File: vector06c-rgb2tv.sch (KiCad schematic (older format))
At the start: 77 parts, among them J1 Conn_01x09, Q1 4.43, U1 CXA2075M, U2 7400, U3 7474, U4 74HC240

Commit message: rename project files, fix Improver's nick
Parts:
- TP1, TP10, TP11, TP12, TP13, TP14, TP15, TP16, TP17, TP18, TP19, TP2, TP3, TP4, TP5, TP6, TP7, TP8, TP9: footprint improve-rgb2tv:PAD-150-60 -> vector06c-rgb2tv:PAD-150-60
- U1: symbol improve-rgb2tv-symbols:CXA2075M -> vector06c-rgb2tv-symbols:CXA2075M
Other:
- note removed: "<-- funny value"
- note removed: "^-- funny value"
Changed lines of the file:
@@
 EESchema Schematic File Version 4
-LIBS:improve-rgb2tv-cache
+LIBS:vector06c-rgb2tv-cache
 EELAYER 29 0
 EELAYER END
@@
 F 0 "TP3" V 1500 4700 50  0001 C CNN
 F 1 "9D5" V 1400 4800 50  0000 L CNN
-F 2 "improve-rgb2tv:PAD-150-60" H 1600 4600 50  0001 C CNN
+F 2 "vector06c-rgb2tv:PAD-150-60" H 1600 4600 50  0001 C CNN
 F 3 "~" H 1600 4600 50  0001 C CNN
 	1    1400 4600
@@
 F 0 "TP4" V 1500 5700 50  0001 C CNN
 F 1 "4D3" V 1400 5800 50  0000 L CNN
-F 2 "improve-rgb2tv:PAD-150-60" H 1600 5600 50  0001 C CNN
+F 2 "vector06c-rgb2tv:PAD-150-60" H 1600 5600 50  0001 C CNN
 F 3 "~" H 1600 5600 50  0001 C CNN
 	1    1400 5600
@@
 F 0 "TP5" V 1500 6000 50  0001 C CNN
 F 1 "6D3" V 1400 6100 50  0000 L CNN
-F 2 "improve-rgb2tv:PAD-150-60" H 1600 5900 50  0001 C CNN
+F 2 "vector06c-rgb2tv:PAD-150-60" H 1600 5900 50  0001 C CNN
 F 3 "~" H 1600 5900 50  0001 C CNN
 	1    1400 5900
@@
 F 0 "TP2" V 1500 4300 50  0001 C CNN
 F 1 "12D4" V 1400 4400 50  0000 L CNN
-F 2 "improve-rgb2tv:PAD-150-60" H 1600 4200 50  0001 C CNN
+F 2 "vector06c-rgb2tv:PAD-150-60" H 1600 4200 50  0001 C CNN
 F 3 "~" H 1600 4200 50  0001 C CNN
 	1    1400 4200
@@
 F 0 "TP1" V 1500 4150 50  0001 C CNN
 F 1 "8D8" V 1400 4250 50  0000 L CNN
-F 2 "improve-rgb2tv:PAD-150-60" H 1600 4050 50  0001 C CNN
+F 2 "vector06c-rgb2tv:PAD-150-60" H 1600 4050 50  0001 C CNN
 F 3 "~" H 1600 4050 50  0001 C CNN
 	1    1400 4050
@@
 F 0 "TP6" V 4950 4250 50  0001 C CNN
 F 1 "SYNC" V 4850 4350 50  0000 L CNN
-F 2 "improve-rgb2tv:PAD-150-60" H 5050 4150 50  0001 C CNN
+F 2 "vector06c-rgb2tv:PAD-150-60" H 5050 4150 50  0001 C CNN
 F 3 "~" H 5050 4150 50  0001 C CNN
 	1    4850 4150
@@
 Connection ~ 7050 1350
 $Comp
-L improve-rgb2tv-symbols:CXA2075M U1
+L vector06c-rgb2tv-symbols:CXA2075M U1
 U 1 1 5EEEF62F
 P 7150 2800
@@
 F 0 "TP7" V 9550 2600 50  0001 C CNN
 F 1 "CVOUT" V 9450 2700 50  0000 L CNN
-F 2 "improve-rgb2tv:PAD-150-60" H 9650 2500 50  0001 C CNN
+F 2 "vector06c-rgb2tv:PAD-150-60" H 9650 2500 50  0001 C CNN
 F 3 "~" H 9650 2500 50  0001 C CNN
 	1    9450 2500
@@
 Wire Wire Line
 	6550 5700 6550 5650
-Text Notes 7250 5150 0    50   ~ 0
-<-- funny value
-Text Notes 8050 3250 0    50   ~ 0
-^-- funny value
 Wire Wire Line
 	8950 5200 8950 5100
@@
 F 0 "TP10" V 1250 1350 50  0001 C CNN
 F 1 "GND" V 1150 1450 50  0000 L CNN
-F 2 "improve-rgb2tv:PAD-150-60" H 1350 1250 50  0001 C CNN
+F 2 "vector06c-rgb2tv:PAD-150-60" H 1350 1250 50  0001 C CNN
 F 3 "~" H 1350 1250 50  0001 C CNN
 	1    1150 1250
@@
 F 0 "TP9" V 1250 1200 50  0001 C CNN
 F 1 "GND" V 1150 1300 50  0000 L CNN
-F 2 "improve-rgb2tv:PAD-150-60" H 1350 1100 50  0001 C CNN
+F 2 "vector06c-rgb2tv:PAD-150-60" H 1350 1100 50  0001 C CNN
 F 3 "~" H 1350 1100 50  0001 C CNN
 	1    1150 1100
@@
 F 0 "TP8" V 1250 1050 50  0001 C CNN
 F 1 "+5V" V 1150 1150 50  0000 L CNN
-F 2 "improve-rgb2tv:PAD-150-60" H 1350 950 50  0001 C CNN
+F 2 "vector06c-rgb2tv:PAD-150-60" H 1350 950 50  0001 C CNN
 F 3 "~" H 1350 950 50  0001 C CNN
 	1    1150 950
@@
 F 0 "TP14" V 9550 3550 50  0001 C CNN
 F 1 "YOUT" V 9450 3650 50  0000 L CNN
-F 2 "improve-rgb2tv:PAD-150-60" H 9650 3450 50  0001 C CNN
+F 2 "vector06c-rgb2tv:PAD-150-60" H 9650 3450 50  0001 C CNN
 F 3 "~" H 9650 3450 50  0001 C CNN
 	1    9450 3450
@@
 F 0 "TP15" V 9550 3800 50  0001 C CNN
 F 1 "COUT" V 9450 3900 50  0000 L CNN
-F 2 "improve-rgb2tv:PAD-150-60" H 9650 3700 50  0001 C CNN
+F 2 "vector06c-rgb2tv:PAD-150-60" H 9650 3700 50  0001 C CNN
 F 3 "~" H 9650 3700 50  0001 C CNN
 	1    9450 3700
@@
 F 0 "TP11" V 9000 1700 50  0001 C CNN
 F 1 "BOUT" V 8900 1800 50  0000 L CNN
-F 2 "improve-rgb2tv:PAD-150-60" H 9100 1600 50  0001 C CNN
+F 2 "vector06c-rgb2tv:PAD-150-60" H 9100 1600 50  0001 C CNN
 F 3 "~" H 9100 1600 50  0001 C CNN
 	1    8900 1600
@@
 F 0 "TP12" V 9000 1900 50  0001 C CNN
 F 1 "GOUT" V 8900 2000 50  0000 L CNN
-F 2 "improve-rgb2tv:PAD-150-60" H 9100 1800 50  0001 C CNN
+F 2 "vector06c-rgb2tv:PAD-150-60" H 9100 1800 50  0001 C CNN
 F 3 "~" H 9100 1800 50  0001 C CNN
 	1    8900 1800
@@
 F 0 "TP13" V 9000 2100 50  0001 C CNN
 F 1 "ROUT" V 8900 2200 50  0000 L CNN
-F 2 "improve-rgb2tv:PAD-150-60" H 9100 2000 50  0001 C CNN
+F 2 "vector06c-rgb2tv:PAD-150-60" H 9100 2000 50  0001 C CNN
 F 3 "~" H 9100 2000 50  0001 C CNN
 	1    8900 2000
@@
 F 0 "TP16" V 1250 1500 50  0001 C CNN
 F 1 "GND" V 1150 1600 50  0000 L CNN
-F 2 "improve-rgb2tv:PAD-150-60" H 1350 1400 50  0001 C CNN
+F 2 "vector06c-rgb2tv:PAD-150-60" H 1350 1400 50  0001 C CNN
 F 3 "~" H 1350 1400 50  0001 C CNN
 	1    1150 1400
@@
 F 0 "TP17" V 1250 1650 50  0001 C CNN
 F 1 "GND" V 1150 1750 50  0000 L CNN
-F 2 "improve-rgb2tv:PAD-150-60" H 1350 1550 50  0001 C CNN
+F 2 "vector06c-rgb2tv:PAD-150-60" H 1350 1550 50  0001 C CNN
 F 3 "~" H 1350 1550 50  0001 C CNN
 	1    1150 1550
@@
 F 0 "TP18" V 1250 1800 50  0001 C CNN
 F 1 "GND" V 1150 1900 50  0000 L CNN
-F 2 "improve-rgb2tv:PAD-150-60" H 1350 1700 50  0001 C CNN
+F 2 "vector06c-rgb2tv:PAD-150-60" H 1350 1700 50  0001 C CNN
 F 3 "~" H 1350 1700 50  0001 C CNN
 	1    1150 1700
@@
 F 0 "TP19" V 1250 1950 50  0001 C CNN
 F 1 "GND" V 1150 2050 50  0000 L CNN
-F 2 "improve-rgb2tv:PAD-150-60" H 1350 1850 50  0001 C CNN
+F 2 "vector06c-rgb2tv:PAD-150-60" H 1350 1850 50  0001 C CNN
 F 3 "~" H 1350 1850 50  0001 C CNN
 	1    1150 1850

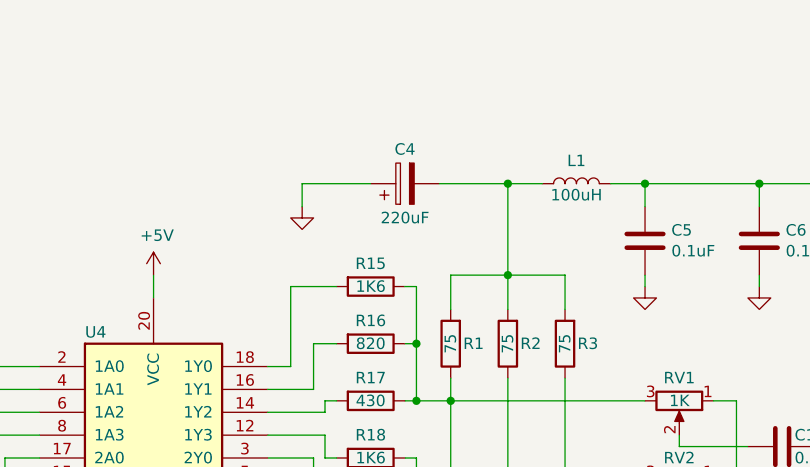
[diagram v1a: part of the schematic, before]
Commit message: fix C4 orientation
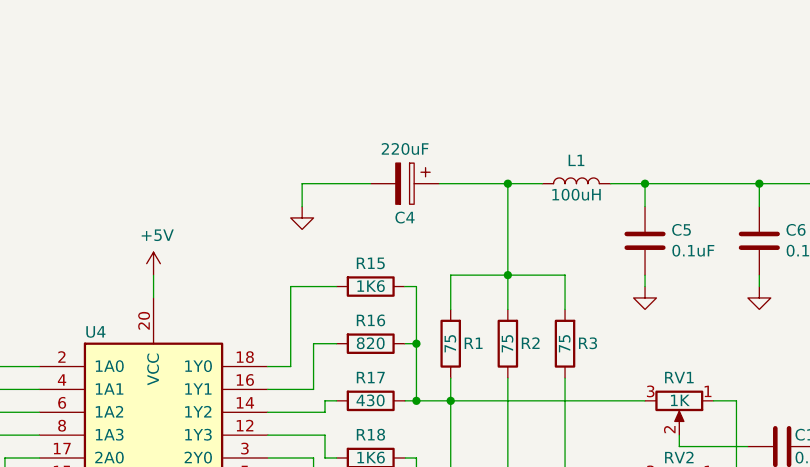
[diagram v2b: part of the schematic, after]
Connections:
- net GND: now also C4.2; no longer C4.1
- net at L1.1, R1.2, R2.2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: now also C4.1; no longer C4.2
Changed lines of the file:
@@
 F 3 "~" H 4150 1350 50  0001 C CNN
 	1    4150 1350
-	0    -1   -1   0
+	0    1    1    0
 $EndComp
 Wire Wire Line
@@
 Wire Wire Line
 	5000 5750 5100 5750
-Wire Wire Line
-	5100 5750 5100 4150
-Wire Wire Line
-	5100 4150 4850 4150
-Connection ~ 5100 4150
-Wire Wire Line
-	5100 4150 5100 3650
-$Comp
-L Connector:TestPoint TP6
-U 1 1 5EE54052
-P 4850 4150
-F 0 "TP6" V 4950 4250 50  0001 C CNN
-F 1 "SYNC" V 4850 4350 50  0000 L CNN
-F 2 "vector06c-rgb2tv:PAD-150-60" H 5050 4150 50  0001 C CNN
-F 3 "~" H 5050 4150 50  0001 C CNN
-	1    4850 4150
-	0    -1   -1   0
-$EndComp
 $Comp
 L Device:L L1
@@
 	8450 4500 8450 3700
 Connection ~ 8450 3700
-Wire Wire Line
-	5400 4500 5250 4500
-Wire Wire Line
-	5250 4500 5250 4700
 $Comp
 L Device:C C12
@@
 	1    0    0    -1
 $EndComp
-Wire Wire Line
-	5250 4700 5700 4700
-Connection ~ 5250 4700
 Wire Wire Line
 	5250 4700 5250 4750
@@
 Wire Wire Line
 	7900 1600 8500 1600
+Connection ~ 5250 4700
+Wire Wire Line
+	5250 4700 5700 4700
+Wire Wire Line
+	5100 4150 5100 3650
+Wire Wire Line
+	5250 4500 5250 4700
+Wire Wire Line
+	5400 4500 5250 4500
+$Comp
+L Connector:TestPoint TP6
+U 1 1 5EE54052
+P 4850 4150
+F 0 "TP6" V 4950 4250 50  0001 C CNN
+F 1 "SYNC" V 4850 4350 50  0000 L CNN
+F 2 "vector06c-rgb2tv:PAD-150-60" H 5050 4150 50  0001 C CNN
+F 3 "~" H 5050 4150 50  0001 C CNN
+	1    4850 4150
+	0    -1   -1   0
+$EndComp
+Connection ~ 5100 4150
+Wire Wire Line
+	5100 4150 4850 4150
+Wire Wire Line
+	5100 5750 5100 4150
 $EndSCHEMATC
